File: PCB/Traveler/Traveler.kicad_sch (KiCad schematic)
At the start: 41 parts, among them J1 Conn_01x06_motFL, J2 Conn_01x06_motFR, J3 Conn_01x06_motBL, J4 Conn_01x06_motBR, J5 Conn_batt, U1 ESP32-DEVKITC, U2 12v-5v, U4 DRV8411APWPR, U5 DRV8411APWPR

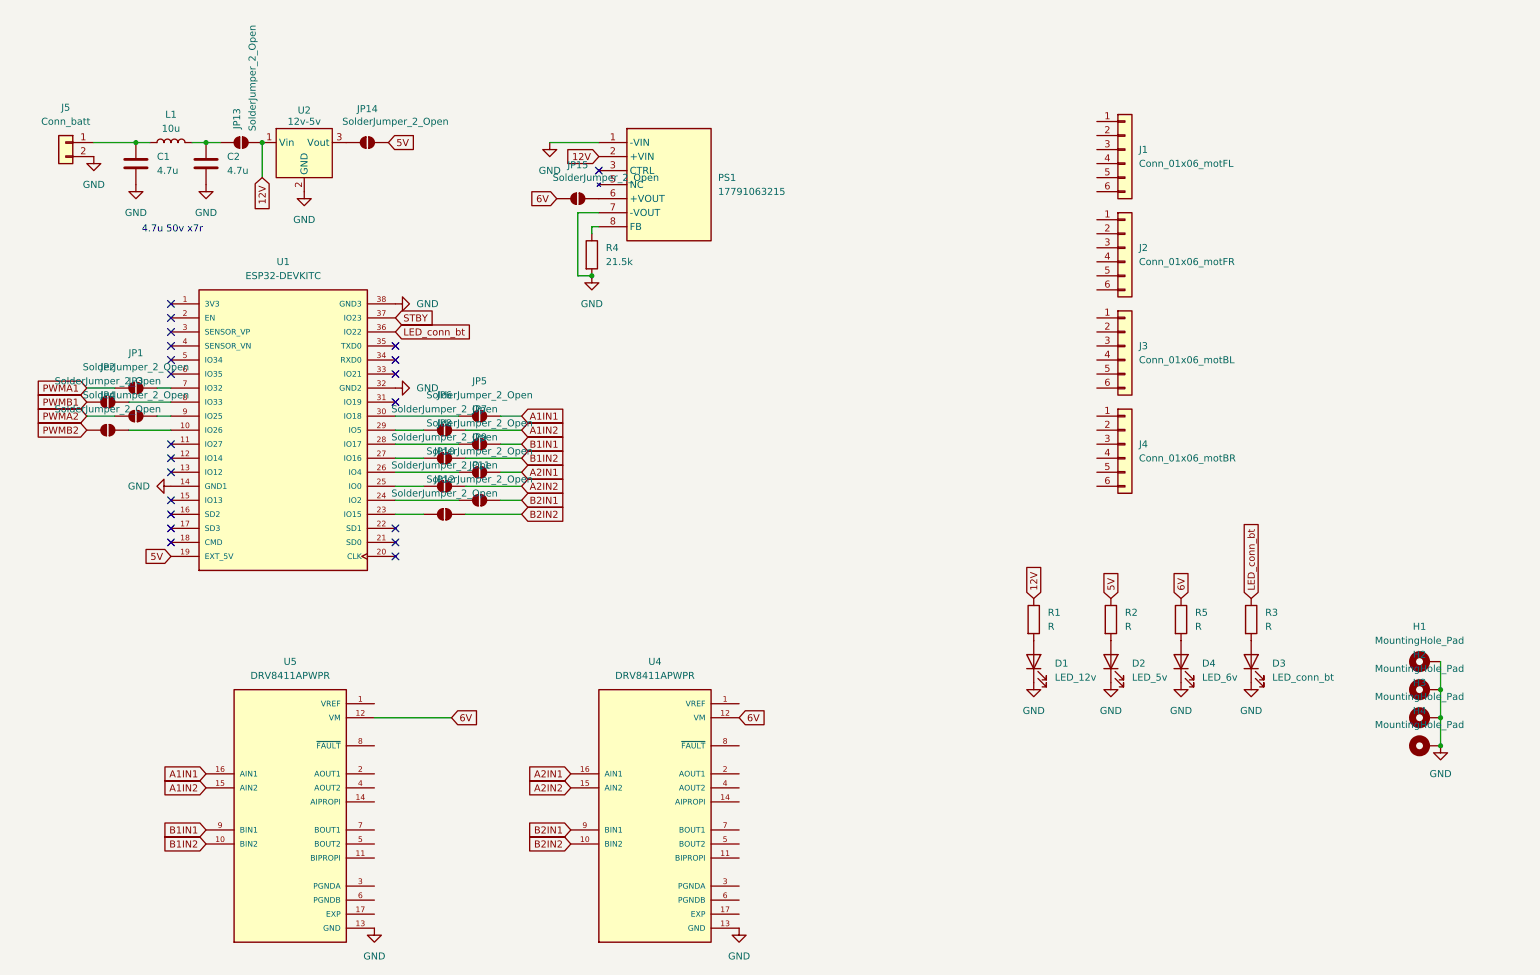
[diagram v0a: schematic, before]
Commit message: Finition de pcb, prèt pour verification
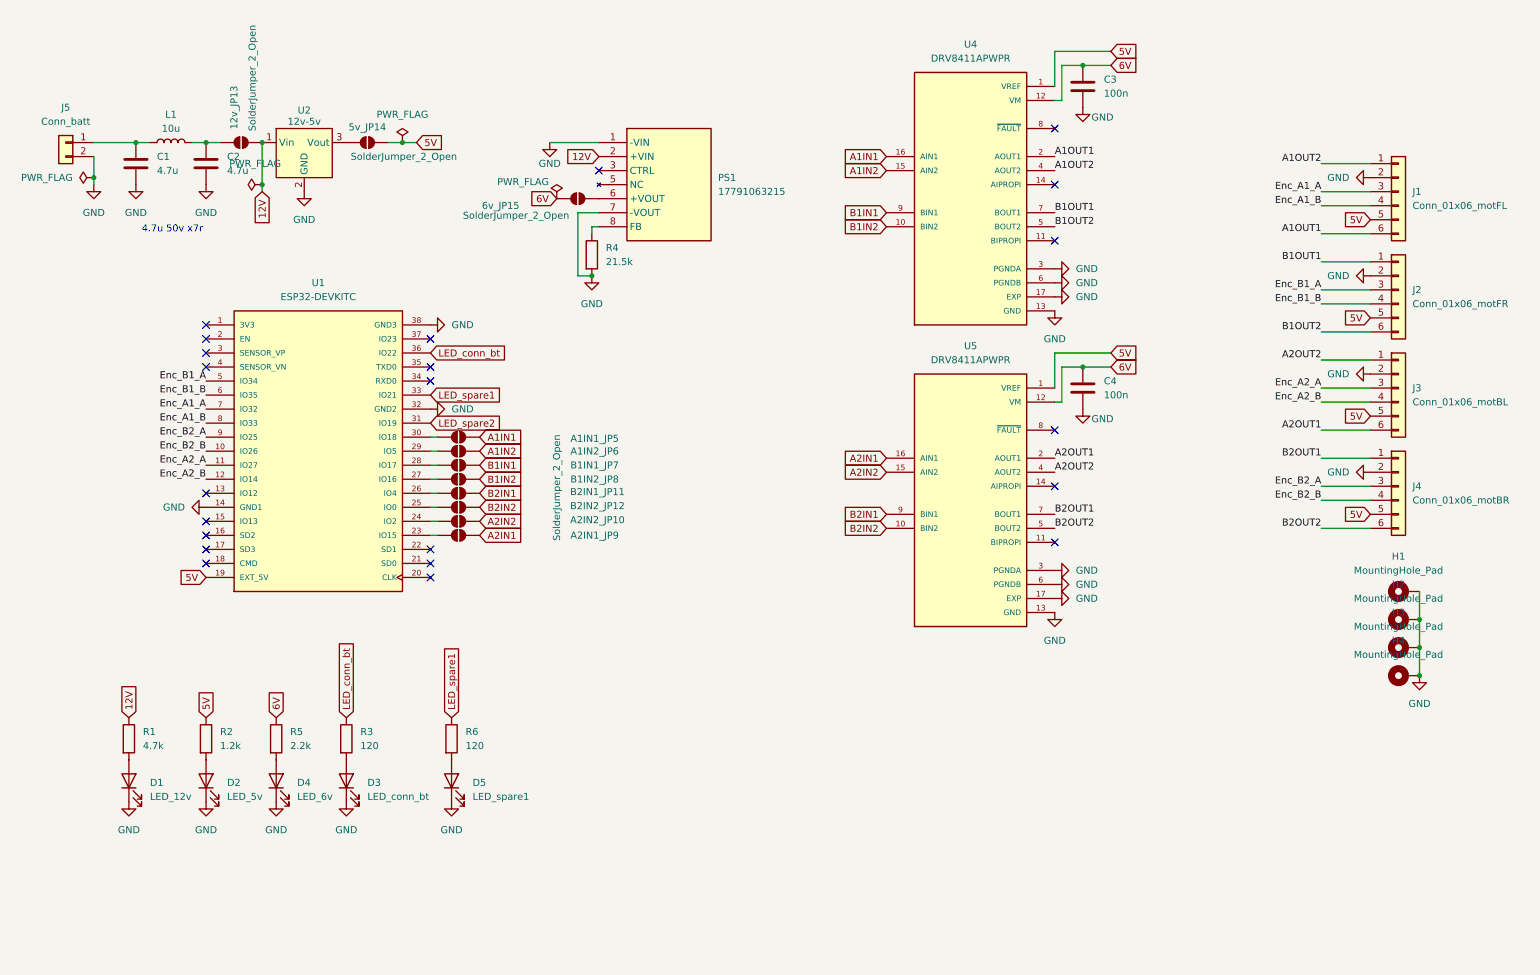
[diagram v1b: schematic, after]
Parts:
- removed JP1, JP2, JP3, JP4: SolderJumper_2_Open, Jumper:SolderJumper-2_P1.3mm_Open_TrianglePad1.0x1.5mm, symbol Jumper:SolderJumper_2_Open
- added C3, C4: 100n, Capacitor_SMD:C_0603_1608Metric, symbol Device:C
- added D5: LED_spare1, LED_SMD:LED_0603_1608Metric_Pad1.05x0.95mm_HandSolder, symbol Device:LED
- added R6: 120, Resistor_SMD:R_0603_1608Metric, symbol Device:R
- C1, C2: footprint (none) -> Capacitor_SMD:C_0603_1608Metric
- H1, H2, H3, H4: footprint (none) -> MountingHole:MountingHole_2.7mm_Pad_TopBottom
- J5: footprint (none) -> Connector_JST:JST_EH_B2B-EH-A_1x02_P2.50mm_Vertical
- L1: footprint (none) -> Capa:capa1
- PS1: footprint 17791063215 -> 17791063215:17791063215
- R1: value R -> 4.7k
- R2: value R -> 1.2k
- R3: value R -> 120
- R5: value R -> 2.2k
- renumbered JP13 to 12v_JP13, JP14 to 5v_JP14, JP15 to 6v_JP15, JP5 to A1IN1_JP5, JP6 to A1IN2_JP6, JP9 to A2IN1_JP9, JP10 to A2IN2_JP10, JP7 to B1IN1_JP7, JP8 to B1IN2_JP8, JP11 to B2IN1_JP11, JP12 to B2IN2_JP12
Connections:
- net 5V: now also J1.5 (Pin_5), J2.5 (Pin_5), J3.5 (Pin_5), J4.5 (Pin_5), U4.1 (VREF), U5.1 (VREF)
- net 6V: now also 6v_JP15.2 (B), C3.1, C4.1; no longer 6v_JP15.1 (A)
- net A1IN1: now also U4.16 (AIN1); no longer U5.16 (AIN1)
- net A1IN2: now also U4.15 (AIN2); no longer U5.15 (AIN2)
- net A2IN1: now also U5.16 (AIN1); no longer U4.16 (AIN1)
- net A2IN2: now also U5.15 (AIN2); no longer U4.15 (AIN2)
- net B1IN1: now also U4.9 (BIN1); no longer U5.9 (BIN1)
- net B1IN2: now also U4.10 (BIN2); no longer U5.10 (BIN2)
- net B2IN1: now also U5.9 (BIN1); no longer U4.9 (BIN1)
- net B2IN2: now also U5.10 (BIN2); no longer U4.10 (BIN2)
- net GND: now also J1.2 (Pin_2), J2.2 (Pin_2), J3.2 (Pin_2), J4.2 (Pin_2), U4.17 (EXP), U4.3 (PGNDA), U4.6 (PGNDB), U5.17 (EXP), U5.3 (PGNDA), U5.6 (PGNDB), C3.2, C4.2, D5.1 (K)
- net Enc_B2_B: now reaches U1.10 (IO26)
- net Enc_B2_B: now also J4.4 (Pin_4)
- net Enc_A2_A: now reaches U1.11 (IO27)
- net Enc_A2_A: now also J3.3 (Pin_3)
- net Enc_A2_B: now reaches U1.12 (IO14)
- net Enc_A2_B: now also J3.4 (Pin_4)
- net at U1.23 (IO15): now also A2IN1_JP9.1 (A); no longer B2IN2_JP12.1 (A)
- net at U1.24 (IO2): now also A2IN2_JP10.1 (A); no longer B2IN1_JP11.1 (A)
- net at U1.25 (IO0): now also B2IN2_JP12.1 (A); no longer A2IN2_JP10.1 (A)
- net at U1.26 (IO4): now also B2IN1_JP11.1 (A); no longer A2IN1_JP9.1 (A)
- net LED_spare2: now reaches U1.31 (IO19)
- net LED_spare1: now reaches U1.33 (IO21)
- net LED_spare1: now also R6.1
- net Enc_B1_A: now reaches U1.5 (IO34)
- net Enc_B1_A: now also J2.3 (Pin_3)
- net Enc_B1_B: now reaches U1.6 (IO35)
- net Enc_B1_B: now also J2.4 (Pin_4)
- net Enc_A1_A: now reaches U1.7 (IO32)
- net Enc_A1_A: now also J1.3 (Pin_3)
- net Enc_A1_B: now reaches U1.8 (IO33)
- net Enc_A1_B: now also J1.4 (Pin_4)
- net Enc_B2_A: now reaches U1.9 (IO25)
- net Enc_B2_A: now also J4.3 (Pin_3)
- net at PS1.6 (+VOUT): now also 6v_JP15.1 (A); no longer 6v_JP15.2 (B)
- net B2OUT1: now reaches J4.1 (Pin_1)
- net B2OUT1: now also U5.7 (BOUT1)
- net B2OUT2: now reaches J4.6 (Pin_6)
- net B2OUT2: now also U5.5 (BOUT2)
- net B1OUT1: now reaches J2.1 (Pin_1)
- net B1OUT1: now also U4.7 (BOUT1)
- net B1OUT2: now reaches J2.6 (Pin_6)
- net B1OUT2: now also U4.5 (BOUT2)
- net A1OUT2: now reaches J1.1 (Pin_1)
- net A1OUT2: now also U4.4 (AOUT2)
- net A1OUT1: now reaches J1.6 (Pin_6)
- net A1OUT1: now also U4.2 (AOUT1)
- net A2OUT2: now reaches J3.1 (Pin_1)
- net A2OUT2: now also U5.4 (AOUT2)
- net A2OUT1: now reaches J3.6 (Pin_6)
- net A2OUT1: now also U5.2 (AOUT1)
- net STBY: no longer names the net of U1.37 (IO23)
- new net: D5.2 (A), R6.2
- no-connect marks 21 -> 22
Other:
- moved on the sheet: A1IN1_JP5, A1IN2_JP6, A2IN1_JP9, A2IN2_JP10, B1IN1_JP7, B1IN2_JP8, B2IN1_JP11, B2IN2_JP12, D1, D2, D3, D4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
